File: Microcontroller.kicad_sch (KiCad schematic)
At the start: 1 part

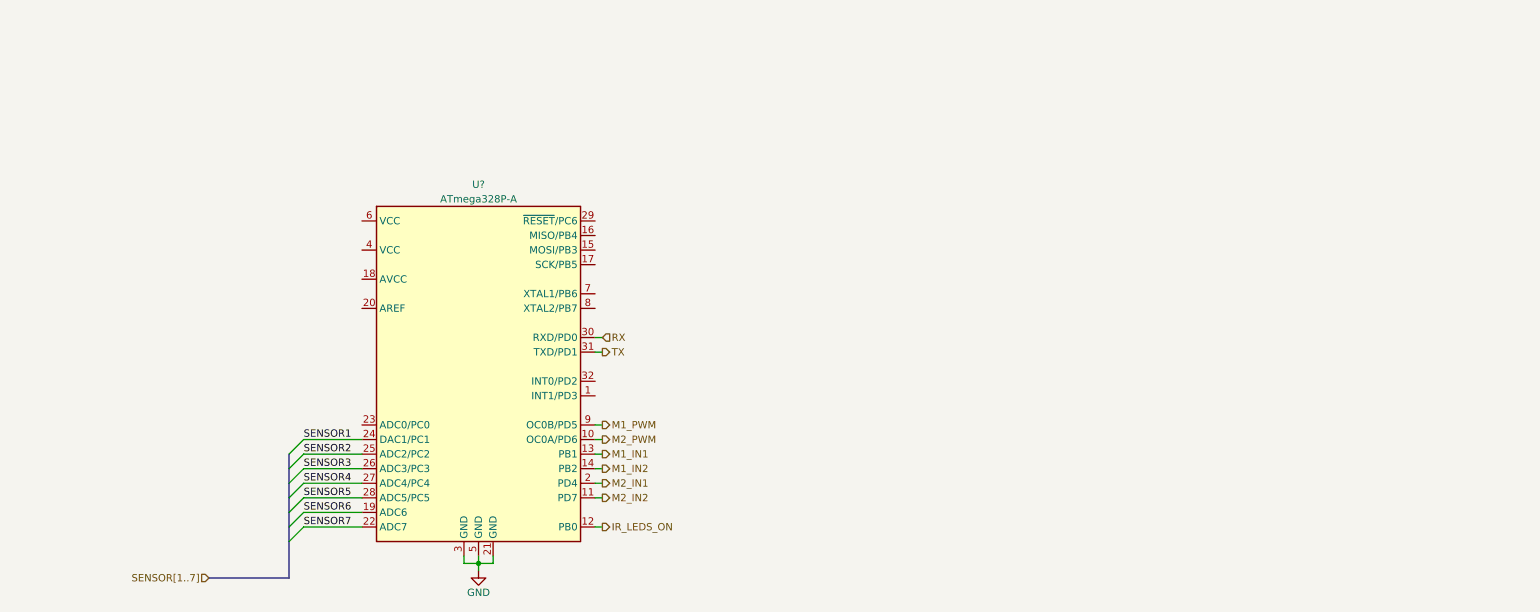
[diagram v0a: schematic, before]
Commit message: Microcontroller schematic
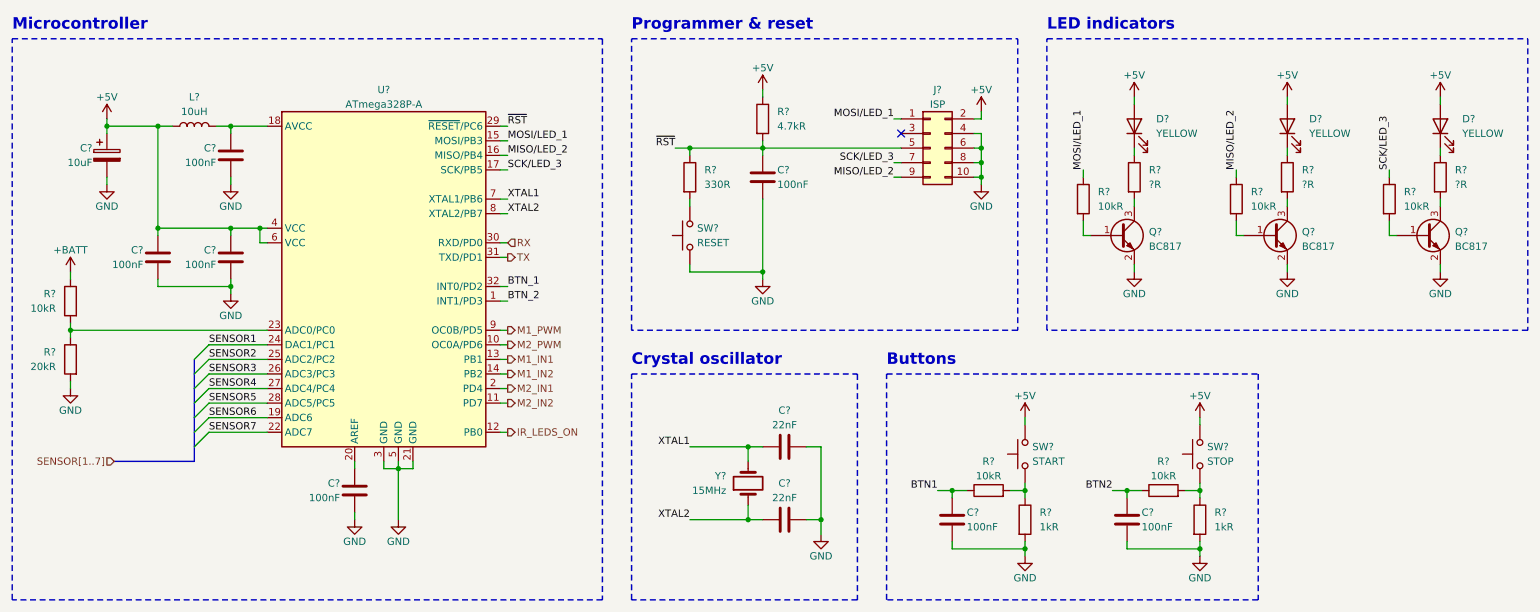
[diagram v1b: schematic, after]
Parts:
- added C? (x7): 100nF, symbol Device:C
- added C? (x2): 22nF, symbol Device:C
- added C?: 10uF, symbol Device:C_Polarized
- added D? (x3): YELLOW, symbol Device:LED
- added J?: ISP, Connector_IDC:IDC-Header_2x05_P2.54mm_Vertical, symbol Connector_Generic:Conn_02x05_Odd_Even
- added L?: 10uH, symbol Device:L
- added Q? (x3): BC817, Package_TO_SOT_SMD:SOT-23, symbol Transistor_BJT:BC817
- added R? (x6): 10kR, symbol Device:R
- added R? (x2): 1kR, symbol Device:R
- added R? (x3): ?R, symbol Device:R
- added R?: 4.7kR, symbol Device:R
- added R?: 330R, symbol Device:R
- added R?: 20kR, symbol Device:R
- added SW?: START, symbol Switch:SW_Push
- added SW?: RESET, symbol Switch:SW_Push
- added SW?: STOP, symbol Switch:SW_Push
- added Y?: 15MHz, symbol Device:Crystal
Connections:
- net GND: now also C?.2, C?.2, C?.2, C?.2, C?.2, C?.2, C?.2, C?.2, C?.2, C?.2, J?.10 (Pin_10), J?.4 (Pin_4), J?.6 (Pin_6), J?.8 (Pin_8), Q?.2 (E), Q?.2 (E), Q?.2 (E), R?.2, R?.2, R?.2, SW?.1
- net BTN_2: now reaches U?.1 (INT1/PD3)
- net MOSI/LED_1: now reaches U?.15 (MOSI/PB3)
- net MOSI/LED_1: now also J?.1 (Pin_1), R?.1
- net MISO/LED_2: now reaches U?.16 (MISO/PB4)
- net MISO/LED_2: now also J?.9 (Pin_9), R?.1
- net SCK/LED_3: now reaches U?.17 (SCK/PB5)
- net SCK/LED_3: now also J?.7 (Pin_7), R?.1
- net at U?.18 (AVCC): now also C?.1, L?.2
- net at U?.20 (AREF): now also C?.1
- net at U?.23 (ADC0/PC0): now also R?.1, R?.2
- net ~{RST}: now reaches U?.29 (~{RESET}/PC6)
- net ~{RST}: now also C?.1, J?.5 (Pin_5), R?.1, R?.2
- net BTN_1: now reaches U?.32 (INT0/PD2)
- net +5V: now reaches U?.4 (VCC)
- net +5V: now also U?.6 (VCC), C?.1, C?.1, C?.1, D?.2 (A), D?.2 (A), D?.2 (A), J?.2 (Pin_2), L?.1, R?.1, SW?.2, SW?.2
- net XTAL1: now reaches U?.7 (XTAL1/PB6)
- net XTAL1: now also C?.1, Y?.2
- net XTAL2: now reaches U?.8 (XTAL2/PB7)
- net XTAL2: now also C?.1, Y?.1
- new net: R?.1, R?.2, SW?.1 (x2)
- new net: D?.1 (K), R?.1 (x3)
- new net: R?.2, SW?.2
- new net: Q?.1 (B), R?.2 (x3)
- new net: Q?.3 (C), R?.2 (x3)
- new net +BATT: R?.1
- new net BTN1: C?.1, R?.1
- new net BTN2: C?.1, R?.1
- no-connect marks 0 -> 1
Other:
- note added: "Buttons"
- note added: "Crystal oscillator"
- note added: "LED indicators"
- note added: "Microcontroller"
- note added: "Programmer & reset"
- moved on the sheet: U?

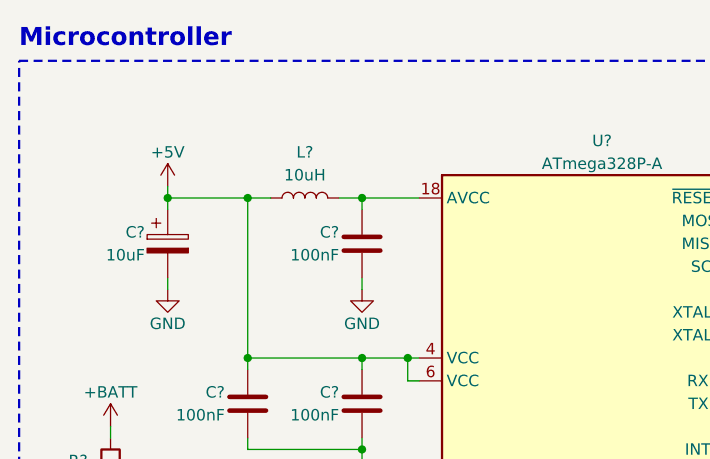
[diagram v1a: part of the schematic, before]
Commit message: Ferrite bead added to uC AVCC pin
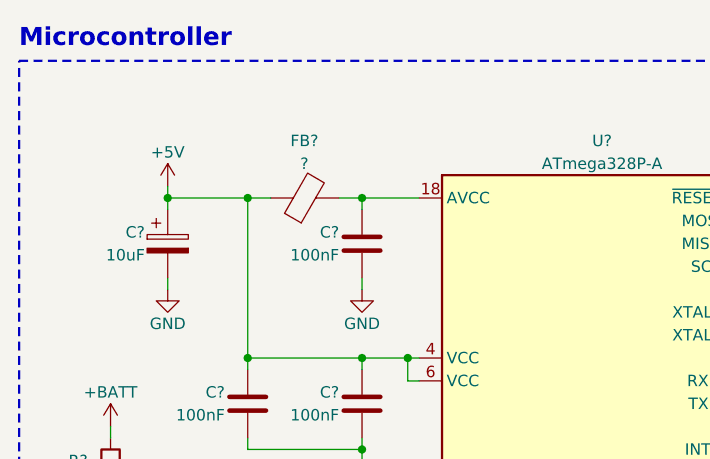
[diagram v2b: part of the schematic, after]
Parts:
- removed L?: 10uH, symbol Device:L
- added FB?: ?, symbol Device:FerriteBead
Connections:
- net +5V: now also FB?.1
- net at C?.1, U?.18 (AVCC): now also FB?.2
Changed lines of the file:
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@@
+    )
+  )
+  (symbol (lib_id "Device:FerriteBead") (at 48.26 34.29 90) (unit 1)
+    (in_bom yes) (on_board yes) (dnp no) (fields_autoplaced)
+    (property "Reference" "FB?" (at 48.2092 27.94 90)
+      (effects (font (size 1.27 1.27)))
+    )
+    (property "Value" "?" (at 48.2092 30.48 90)
+      (effects (font (size 1.27 1.27)))
+    )
+    (property "Footprint" "" (at 48.26 36.068 90)
+      (effects (font (size 1.27 1.27)) hide)
+    )
+    (property "Datasheet" "~" (at 48.26 34.29 0)
+      (effects (font (size 1.27 1.27)) hide)
+    )
+    (pin "1")
+    (pin "2")
+    (instances
+      (project "Autko"
+        (path "/8d5cfdec-de34-4148-9100-7125640c46f5/bbdb254f-809b-458f-9d25-868d15ad41c7"
+          (reference "FB?") (unit 1)
+        )
+      )
     )
   )
@@
         )
       )
-    )
-  )
-  (symbol (lib_id "Device:L") (at 48.26 34.29 90) (unit 1)
-    (in_bom yes) (on_board yes) (dnp no)
-    (property "Reference" "L?" (at 48.26 29.21 90)
-      (effects (font (size 1.27 1.27)))
-    )
-    (property "Value" "10uH" (at 48.26 31.75 90)
-      (effects (font (size 1.27 1.27)))
-    )
-    (property "Footprint" "" (at 48.26 34.29 0)
-      (effects (font (size 1.27 1.27)) hide)
-    )
-    (property "Datasheet" "~" (at 48.26 34.29 0)
-      (effects (font (size 1.27 1.27)) hide)
-    )
-    (pin "1")
-    (pin "2")
-    (instances
-      (project "Autko"
-        (path "/8d5cfdec-de34-4148-9100-7125640c46f5/bbdb254f-809b-458f-9d25-868d15ad41c7"
-          (reference "L?") (unit 1)
-        )
-      )

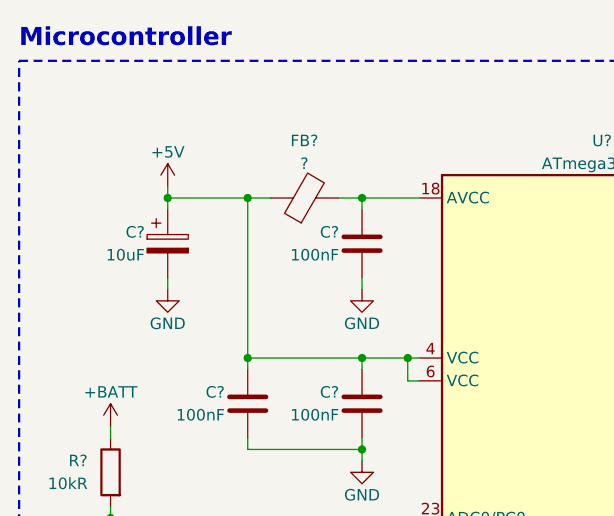
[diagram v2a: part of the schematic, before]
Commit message: 10uF removed from uC power supply
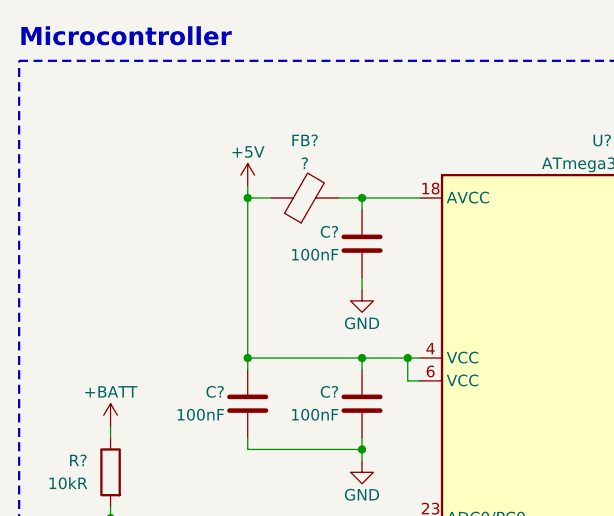
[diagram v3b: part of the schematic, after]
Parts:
- removed C?: 10uF, symbol Device:C_Polarized
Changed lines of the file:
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@@
 (kicad_sch (version 20230121) (generator eeschema)
   (paper "A4")
-  (junction (at 33.02 34.29) (diameter 0) (color 0 0 0 0)
-  )
   (junction (at 147.32 38.1) (diameter 0) (color 0 0 0 0)
   )
@@
     (stroke (width 0) (type default))
   )
+  (wire (pts (xy 41.91 33.02) (xy 41.91 34.29))
+    (stroke (width 0) (type default))
+  )
   (wire (pts (xy 50.8 74.93) (xy 60.96 74.93))
     (stroke (width 0) (type default))
@@
     (stroke (width 0) (type default))
   )
-  (wire (pts (xy 33.02 43.18) (xy 33.02 44.45))
-    (stroke (width 0) (type default))
-  )
   (bus (pts (xy 48.26 87.63) (xy 48.26 90.17))
     (stroke (width 0) (type default))
   )
-  (wire (pts (xy 33.02 34.29) (xy 33.02 35.56))
-    (stroke (width 0) (type default))
-  )
   (wire (pts (xy 54.61 34.29) (xy 54.61 35.56))
     (stroke (width 0) (type default))
@@
     (stroke (width 0) (type default))
   )
-  (wire (pts (xy 33.02 34.29) (xy 41.91 34.29))
-    (stroke (width 0) (type default))
-  )
   (wire (pts (xy 76.2 101.6) (xy 76.2 102.87))
     (stroke (width 0) (type default))
@@
   )
   (wire (pts (xy 50.8 80.01) (xy 60.96 80.01))
-    (stroke (width 0) (type default))
-  )
-  (wire (pts (xy 33.02 33.02) (xy 33.02 34.29))
     (stroke (width 0) (type default))
   )
@@
   )
   (symbol (lib_id "Device:FerriteBead") (at 48.26 34.29 90) (unit 1)
-    (in_bom yes) (on_board yes) (dnp no) (fields_autoplaced)
-    (property "Reference" "FB?" (at 48.2092 27.94 90)
-      (effects (font (size 1.27 1.27)))
-    )
-    (property "Value" "?" (at 48.2092 30.48 90)
+    (in_bom yes) (on_board yes) (dnp no)
+    (property "Reference" "FB?" (at 48.26 27.94 90)
+      (effects (font (size 1.27 1.27)))
+    )
+    (property "Value" "?" (at 48.26 30.48 90)
       (effects (font (size 1.27 1.27)))
     )
@@
         (path "/8d5cfdec-de34-4148-9100-7125640c46f5/bbdb254f-809b-458f-9d25-868d15ad41c7"
           (reference "#PWR017") (unit 1)
-        )
-      )
-    )
-  )
-  (symbol (lib_id "power:GND") (at 33.02 44.45 0) (unit 1)
-    (in_bom yes) (on_board yes) (dnp no)
-    (property "Reference" "#PWR028" (at 33.02 50.8 0)
-      (effects (font (size 1.27 1.27)) hide)
-    )
-    (property "Value" "GND" (at 33.02 48.26 0)
-      (effects (font (size 1.27 1.27)))
-    )
-    (property "Footprint" "" (at 33.02 44.45 0)
-      (effects (font (size 1.27 1.27)) hide)
-    )
-    (property "Datasheet" "" (at 33.02 44.45 0)
-      (effects (font (size 1.27 1.27)) hide)
-    )
-    (pin "1")
-    (instances
-      (project "Autko"
-        (path "/8d5cfdec-de34-4148-9100-7125640c46f5/bbdb254f-809b-458f-9d25-868d15ad41c7"
-          (reference "#PWR028") (unit 1)
         )
       )
@@
     )
   )
-  (symbol (lib_id "power:+5V") (at 33.02 33.02 0) (unit 1)
-    (in_bom yes) (on_board yes) (dnp no) (fields_autoplaced)
-    (property "Reference" "#PWR027" (at 33.02 36.83 0)
-      (effects (font (size 1.27 1.27)) hide)
-    )
-    (property "Value" "+5V" (at 33.02 29.21 0)
-      (effects (font (size 1.27 1.27)))
-    )
-    (property "Footprint" "" (at 33.02 33.02 0)
-      (effects (font (size 1.27 1.27)) hide)
-    )
-    (property "Datasheet" "" (at 33.02 33.02 0)
+  (symbol (lib_id "power:+5V") (at 41.91 33.02 0) (unit 1)
+    (in_bom yes) (on_board yes) (dnp no)
+    (property "Reference" "#PWR027" (at 41.91 36.83 0)
+      (effects (font (size 1.27 1.27)) hide)
+    )
+    (property "Value" "+5V" (at 41.91 29.21 0)
+      (effects (font (size 1.27 1.27)))
+    )
+    (property "Footprint" "" (at 41.91 33.02 0)
+      (effects (font (size 1.27 1.27)) hide)
+    )
+    (property "Datasheet" "" (at 41.91 33.02 0)
       (effects (font (size 1.27 1.27)) hide)
     )
@@
         )
       )
-    )
-  )
-  (symbol (lib_id "Device:C_Polarized") (at 33.02 39.37 0) (unit 1)
-    (in_bom yes) (on_board yes) (dnp no)
-    (property "Reference" "C?" (at 30.48 38.1 0)
-      (effects (font (size 1.27 1.27)) (justify right))
-    )
-    (property "Value" "10uF" (at 30.48 40.64 0)
-      (effects (font (size 1.27 1.27)) (justify right))
-    )
-    (property "Footprint" "" (at 33.9852 43.18 0)
-      (effects (font (size 1.27 1.27)) hide)
-    )
-    (property "Datasheet" "~" (at 33.02 39.37 0)
-      (effects (font (size 1.27 1.27)) hide)
-    )
-    (pin "1")
-    (pin "2")
-    (instances
-      (project "Autko"
-        (path "/8d5cfdec-de34-4148-9100-7125640c46f5/bbdb254f-809b-458f-9d25-868d15ad41c7"
-          (reference "C?") (unit 1)
-        )
-      )

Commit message: Annotate schematics
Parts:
- gave numbers to parts that had none: 36

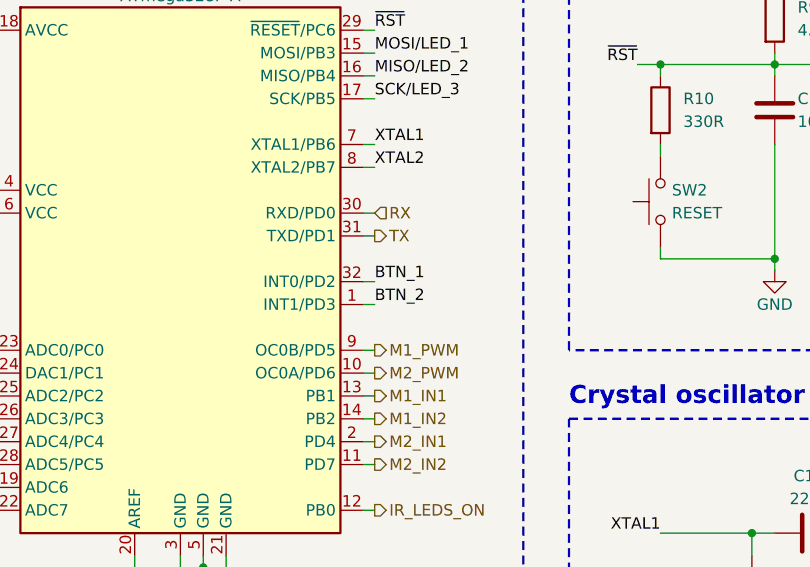
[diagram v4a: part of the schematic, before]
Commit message: ERC fixes
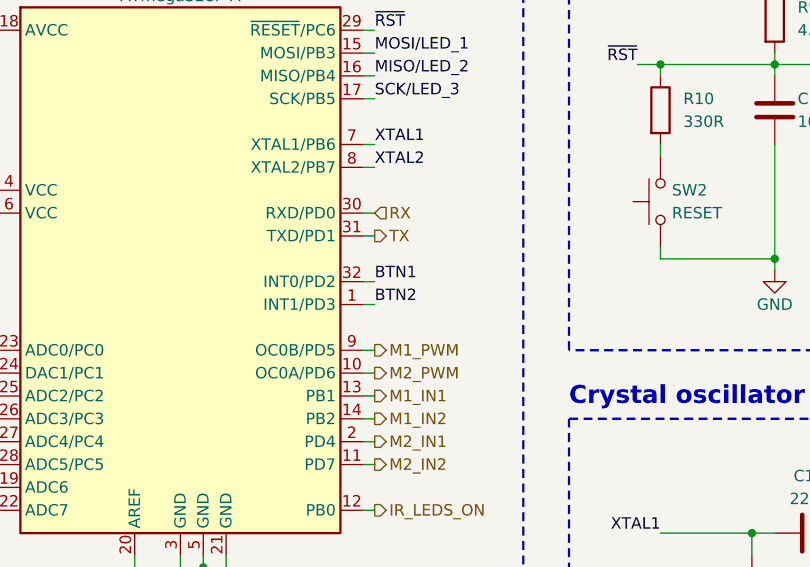
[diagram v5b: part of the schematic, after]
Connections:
- net BTN_1 is gone; now on net BTN1: U4.32 (INT0/PD2)
- net BTN_2 is gone; now on net BTN2: U4.1 (INT1/PD3)
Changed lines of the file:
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@@
     (effects (font (size 1.27 1.27)) (justify left bottom))
   )
-  (label "BTN_2" (at 102.87 64.77 0) (fields_autoplaced)
+  (label "BTN2" (at 102.87 64.77 0) (fields_autoplaced)
     (effects (font (size 1.27 1.27)) (justify left bottom))
   )
-  (label "BTN_1" (at 102.87 62.23 0) (fields_autoplaced)
+  (label "BTN1" (at 102.87 62.23 0) (fields_autoplaced)
     (effects (font (size 1.27 1.27)) (justify left bottom))
   )
